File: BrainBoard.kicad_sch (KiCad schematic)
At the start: 30 parts, among them IC1 STM32G0B1KET6, IC2 MCP2542FDxMF, J2 POWER_IO, J3 COMMS, J4 CAN, U7 TPS62162DSG

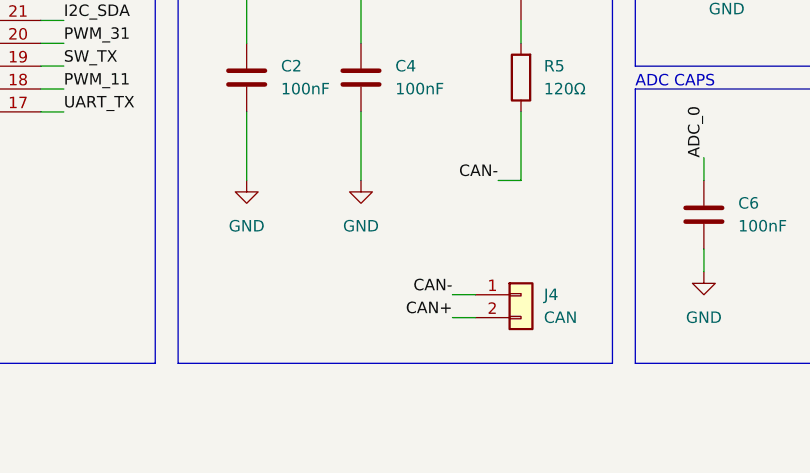
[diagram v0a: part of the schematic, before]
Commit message: Changed CAN port to 3pin;
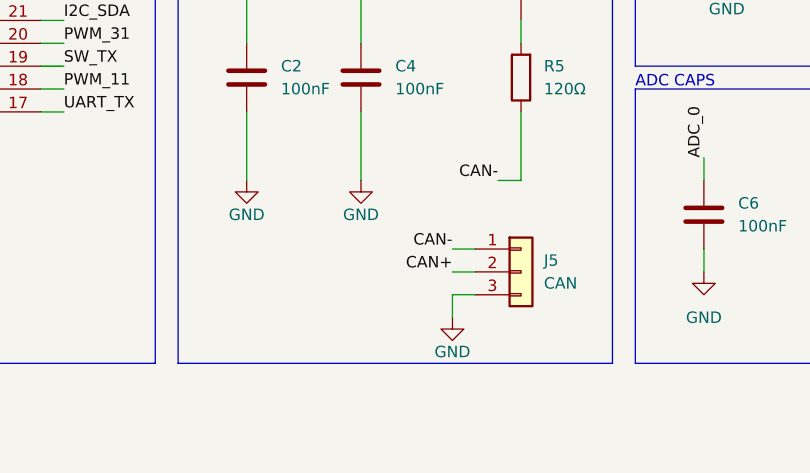
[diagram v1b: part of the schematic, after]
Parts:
- removed J4: CAN, Connector_JST:JST_GH_BM02B-GHS-TBT_1x02-1MP_P1.25mm_Vertical, symbol Connector_Generic:Conn_01x02
- added J5: CAN, Connector_JST:JST_GH_BM03B-GHS-TBT_1x03-1MP_P1.25mm_Vertical, symbol Connector_Generic:Conn_01x03
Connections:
- net CAN+: now also J5.2 (Pin_2)
- net CAN-: now also J5.1 (Pin_1)
- net GND: now also J5.3 (Pin_3)
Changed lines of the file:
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@@
 	(wire
 		(pts
-			(xy 170.18 149.86) (xy 172.72 149.86)
+			(xy 170.18 144.78) (xy 172.72 144.78)
 		)
 		(stroke
@@
 	(wire
 		(pts
+			(xy 170.18 149.86) (xy 170.18 147.32)
+		)
+		(stroke
+			(width 0)
+			(type default)
+		)
+	)
+	(wire
+		(pts
 			(xy 215.9 38.1) (xy 218.44 38.1)
 		)
@@
 	(wire
 		(pts
-			(xy 170.18 147.32) (xy 172.72 147.32)
+			(xy 170.18 142.24) (xy 172.72 142.24)
 		)
 		(stroke
@@
 		)
 	)
+	(wire
+		(pts
+			(xy 170.18 147.32) (xy 172.72 147.32)
+		)
+		(stroke
+			(width 0)
+			(type default)
+		)
+	)
 	(polyline
 		(pts
@@
 	)
 	(label "CAN-"
-		(at 170.18 147.32 180)
+		(at 170.18 142.24 180)
 		(effects
 			(font
@@
 	)
 	(label "CAN+"
-		(at 170.18 149.86 180)
+		(at 170.18 144.78 180)
 		(effects
 			(font
@@
 		(on_board yes)
 		(dnp no)
-		(fields_autoplaced yes)
 		(property "Reference" "#PWR019"
 			(at 160.02 140.97 0)
@@
 		)
 		(property "Value" "GND"
-			(at 160.02 139.7 0)
+			(at 160.02 138.43 0)
 			(effects
 				(font
@@
 	(symbol
 		(lib_id "power:GND")
+		(at 170.18 149.86 0)
+		(unit 1)
+		(exclude_from_sim no)
+		(in_bom yes)
+		(on_board yes)
+		(dnp no)
+		(property "Reference" "#PWR033"
+			(at 170.18 156.21 0)
+			(effects
+				(font
+					(size 1.27 1.27)
+				)
+				(hide yes)
+			)
+		)
+		(property "Value" "GND"
+			(at 170.18 153.67 0)
+			(effects
+				(font
+					(size 1.27 1.27)
+				)
+			)
+		)
+		(property "Footprint" ""
+			(at 170.18 149.86 0)
+			(effects
+				(font
+					(size 1.27 1.27)
+				)
+				(hide yes)
+			)
+		)
+		(property "Datasheet" ""
+			(at 170.18 149.86 0)
+			(effects
+				(font
+					(size 1.27 1.27)
+				)
+				(hide yes)
+			)
+		)
+		(property "Description" "Power symbol creates a global label with name \"GND\" , ground"
+			(at 170.18 149.86 0)
+			(effects
+				(font
+					(size 1.27 1.27)
+				)
+				(hide yes)
+			)
+		)
+		(pin "1"
+		)
+		(instances
+			(project "BrainBoard"
+				(path "/34bda88b-d8fd-4ec8-84e5-47b089adb0f6"
+					(reference "#PWR033")
+					(unit 1)
+				)
+			)
+		)
+	)
+	(symbol
+		(lib_id "power:GND")
 		(at 243.84 144.78 0)
 		(unit 1)
@@
 		(on_board yes)
 		(dnp no)
-		(fields_autoplaced yes)
 		(property "Reference" "#PWR017"
 			(at 147.32 140.97 0)
@@
 		)
 		(property "Value" "GND"
-			(at 147.32 139.7 0)
+			(at 147.32 138.43 0)
 			(effects
 				(font
@@
 	)
 	(symbol
+		(lib_id "Connector_Generic:Conn_01x03")
+		(at 177.8 144.78 0)
+		(unit 1)
+		(exclude_from_sim no)
+		(in_bom yes)
+		(on_board yes)
+		(dnp no)
+		(fields_autoplaced yes)
+		(property "Reference" "J5"
+			(at 180.34 143.5099 0)
+			(effects
+				(font
+					(size 1.27 1.27)
+				)
+				(justify left)
+			)
+		)
+		(property "Value" "CAN"
+			(at 180.34 146.0499 0)
+			(effects
+				(font
+					(size 1.27 1.27)
+				)
+				(justify left)
+			)
+		)
+		(property "Footprint" "Connector_JST:JST_GH_BM03B-GHS-TBT_1x03-1MP_P1.25mm_Vertical"
+			(at 177.8 144.78 0)
+			(effects
+				(font
+					(size 1.27 1.27)
+				)
+				(hide yes)
+			)
+		)
+		(property "Datasheet" "~"
+			(at 177.8 144.78 0)
+			(effects
+				(font
+					(size 1.27 1.27)
+				)
+				(hide yes)
+			)
+		)
+		(property "Description" "Generic connector, single row, 01x03, script generated (kicad-library-utils/schlib/autogen/connector/)"
+			(at 177.8 144.78 0)
+			(effects
+				(font
+					(size 1.27 1.27)
+				)
+				(hide yes)
+			)
+		)
+		(pin "2"
+		)
+		(pin "3"
+		)
+		(pin "1"
+		)
+		(instances
+			(project ""
+				(path "/34bda88b-d8fd-4ec8-84e5-47b089adb0f6"
+					(reference "J5")
+					(unit 1)
+				)
+			)
+		)
+	)
+	(symbol
 		(lib_id "Device:R")
 		(at 241.3 99.06 180)
@@
 					(unit 1)
 				)
-			)
-		)
-	)
-	(symbol
-		(lib_id "Connector_Generic:Conn_01x02")
-		(at 177.8 147.32 0)
-		(unit 1)
-		(exclude_from_sim no)
-		(in_bom yes)
-		(on_board yes)
-		(dnp no)
-		(property "Reference" "J4"
-			(at 180.34 147.3199 0)
-			(effects
-				(font
-					(size 1.27 1.27)
-				)
-				(justify left)
-			)
-		)
-		(property "Value" "CAN"
-			(at 180.34 149.8599 0)
-			(effects
-				(font
-					(size 1.27 1.27)
-				)
-				(justify left)
-			)
-		)
-		(property "Footprint" "Connector_JST:JST_GH_BM02B-GHS-TBT_1x02-1MP_P1.25mm_Vertical"
-			(at 177.8 147.32 0)
-			(effects
-				(font
-					(size 1.27 1.27)
-				)
-				(hide yes)
-			)
-		)
-		(property "Datasheet" "~"
-			(at 177.8 147.32 0)
-			(effects
-				(font
-					(size 1.27 1.27)
-				)
-				(hide yes)
-			)
-		)
-		(property "Description" "Generic connector, single row, 01x02, script generated (kicad-library-utils/schlib/autogen/connector/)"
-			(at 177.8 147.32 0)
-			(effects
-				(font
-					(size 1.27 1.27)
-				)
-				(hide yes)
-			)
-		)
-		(pin "2"
-		)
-		(pin "1"
-		)
-		(instances
-			(project "BrainBoard"
-				(path "/34bda88b-d8fd-4ec8-84e5-47b089adb0f6"
-					(reference "J4")
-					(unit 1)
-				)

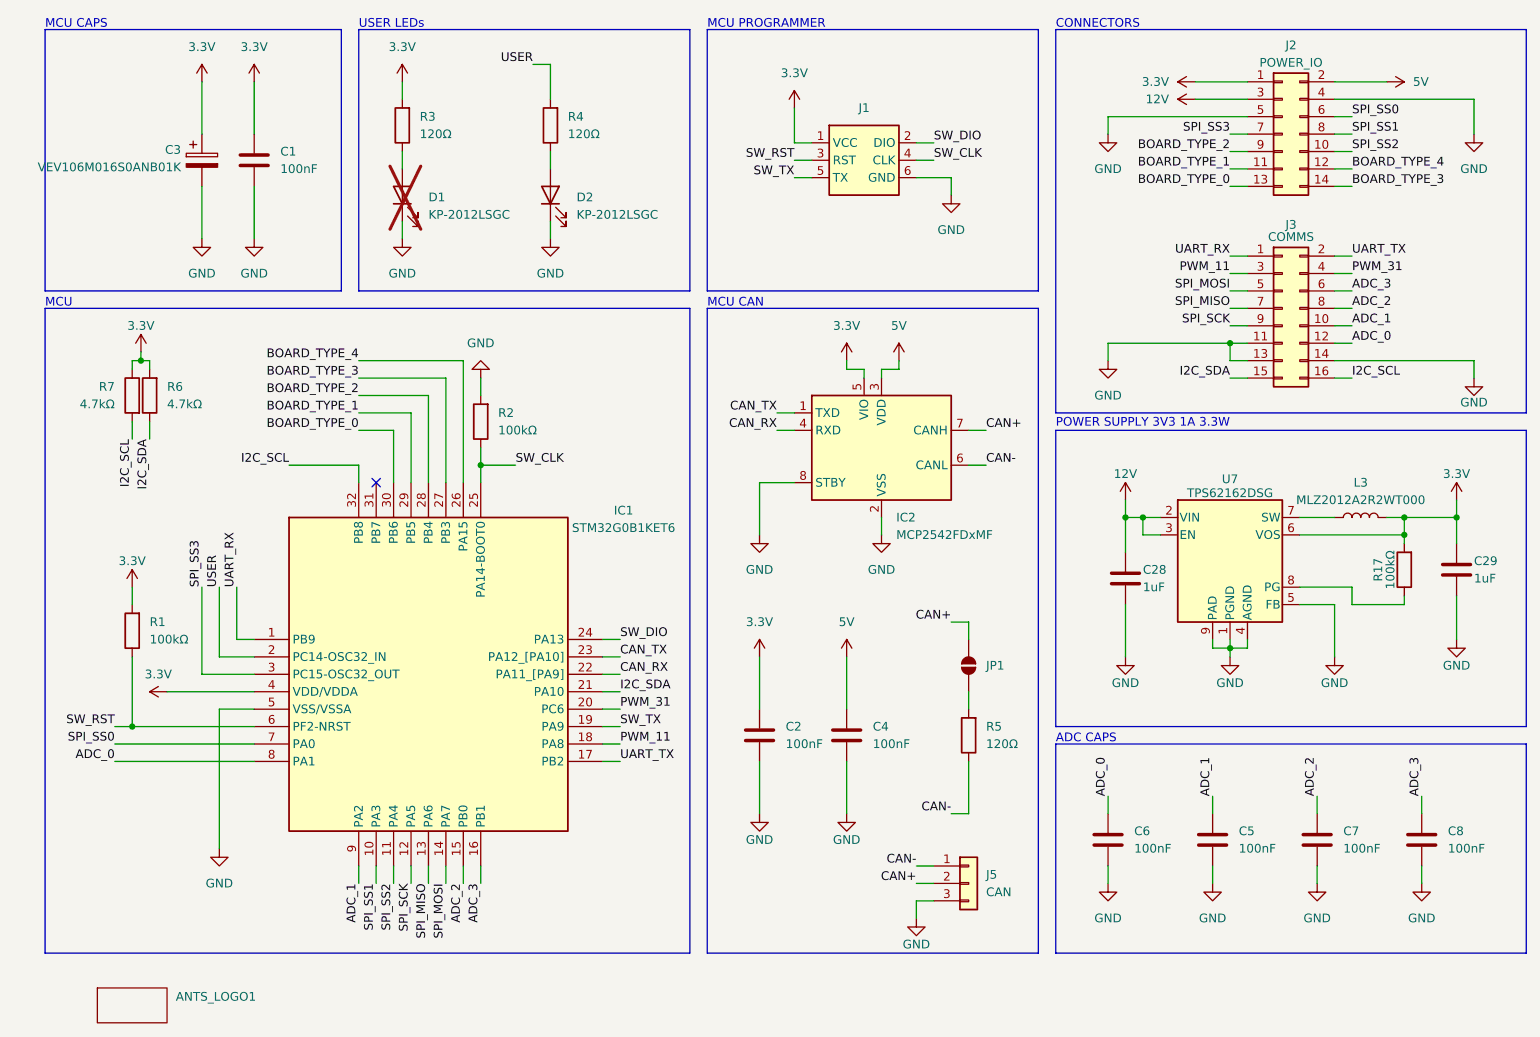
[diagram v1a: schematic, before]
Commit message: Schematic overhaul: Added separated sheets for functions, Added 5V DCDC, Board overhaul: Modified to be MFR ready, Added 5V DCDC,
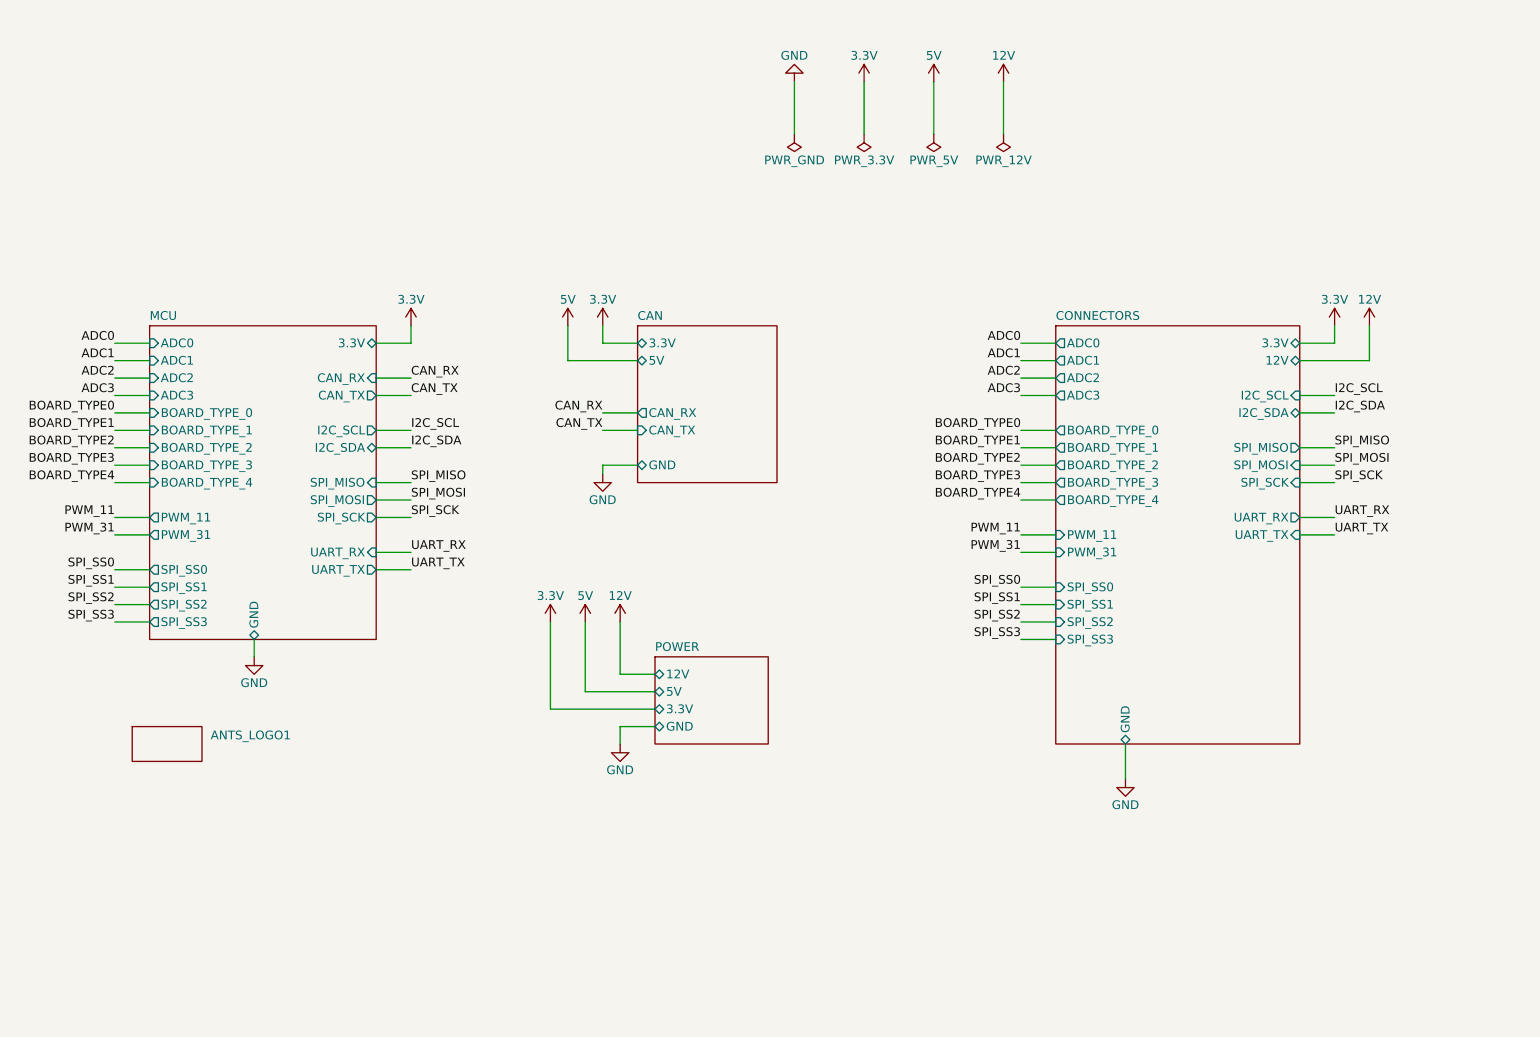
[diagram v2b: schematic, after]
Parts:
- removed C1, C2, C4, C5, C6, C7, C8: 100nF, Capacitor_SMD:C_0805_2012Metric, symbol Device:C
- removed C28, C29: 1uF, Capacitor_SMD:C_0805_2012Metric, symbol Device:C
- removed C3: VEV106M016S0ANB01K, Capacitor_SMD:CP_Elec_4x5.4, symbol Device:C_Polarized
- removed D1, D2: KP-2012LSGC, LED_SMD:LED_0805_2012Metric, symbol Device:LED
- removed IC1: STM32G0B1KET6, Package_QFP:LQFP-32_7x7mm_P0.8mm, symbol STM32G0B1KET6:STM32G0B1KET6
- removed IC2: MCP2542FDxMF, Package_SO:SOIC-8_NO_PAD, symbol Interface_CAN_LIN:MCP2542FDxMF
- removed J1: ~, Connector_PinSocket_2.54mm:PinSocket_2x03_P2.54mm_Vertical, symbol antslab:STM_PROG
- removed J2: POWER_IO, Connector_PinHeader_2.54mm:PinHeader_2x07_P2.54mm_Vertical, symbol Connector_Generic:Conn_02x07_Odd_Even
- removed J3: COMMS, Connector_PinHeader_2.54mm:PinHeader_2x08_P2.54mm_Vertical, symbol Connector_Generic:Conn_02x08_Odd_Even
- removed J5: CAN, Connector_JST:JST_GH_BM03B-GHS-TBT_1x03-1MP_P1.25mm_Vertical, symbol Connector_Generic:Conn_01x03
- removed JP1: SolderJumper_2_Open, Jumper:SolderJumper-2_P1.3mm_Open_RoundedPad1.0x1.5mm, symbol Jumper:SolderJumper_2_Open
- removed L3: MLZ2012A2R2WT000, Inductor_SMD:L_0805_2012Metric, symbol Device:L
- removed R1, R17, R2: 100kΩ, Resistor_SMD:R_0805_2012Metric, symbol Device:R
- removed R3, R4, R5: 120Ω, Resistor_SMD:R_0805_2012Metric, symbol Device:R
- removed R6, R7: 4.7kΩ, Resistor_SMD:R_0805_2012Metric, symbol Device:R
- removed U7: TPS62162DSG, Package_SON:WSON-8-1EP_2x2mm_P0.5mm_EP0.9x1.6mm_ThermalVias, symbol Regulator_Switching:TPS62162DSG
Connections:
- no-connect marks 1 -> 0
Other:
- added sheet CAN (can.kicad_sch)
- added sheet CONNECTORS (connectors.kicad_sch)
- added sheet MCU (mcu.kicad_sch)
- added sheet POWER (power.kicad_sch)
- note removed: "ADC CAPS"
- note removed: "CONNECTORS"
- note removed: "MCU"
- note removed: "MCU CAN"
- note removed: "MCU CAPS"
- note removed: "MCU PROGRAMMER"
- note removed: "POWER SUPPLY 3V3 1A 3.3W"
- note removed: "USER LEDs"
- moved on the sheet: ANTS_LOGO1
